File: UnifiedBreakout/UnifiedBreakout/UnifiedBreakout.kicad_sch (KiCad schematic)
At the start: 29 parts, among them J6 24V BUS, J7 DRAWBAR+MIST+AXIS_PWR, J8 LIMIT, J9 AUX, U4 G3VM-61A1, U5 G3VM-61A1, U6 G3VM-61A1, U7 4N35

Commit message: V3 BOM
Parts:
- C2, C4: Farnell PN (none) -> 8126585; MPN 860080574007 -> 35RX30100M8X11.5; Manufacturer Wurth Elektronik -> Rubycon
- R11, R12, R16: Farnell PN (none) -> 9341528; MPN CFR-25JB-52-220R -> MF25 220R; Manufacturer Yageo -> MULTICOMP PRO
- R13, R14, R15, R18: Farnell PN (none) -> 9341536; MPN CFR-25JB-52-2K2 -> MF25 2K2; Manufacturer Yageo -> MULTICOMP PRO
- R17: Farnell PN (none) -> 9341552; MPN CFR-25JB-52-220K -> MF25 220K; Manufacturer Yageo -> MULTICOMP PRO
- U4, U5, U6: MPN (none) -> G3VM-61A1; Manufacturer (none) -> Omron
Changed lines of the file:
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@@
       (effects (font (size 1.27 1.27)) hide)
     )
-    (property "MPN" "860080574007" (at 124.46 270.51 0)
-      (effects (font (size 1.27 1.27)) hide)
-    )
-    (property "Manufacturer" "Wurth Elektronik" (at 124.46 270.51 0)
-      (effects (font (size 1.27 1.27)) hide)
-    )
-    (property "Farnell PN" "" (at 124.46 270.51 0)
+    (property "MPN" "35RX30100M8X11.5 " (at 124.46 270.51 0)
+      (effects (font (size 1.27 1.27)) hide)
+    )
+    (property "Manufacturer" "Rubycon" (at 124.46 270.51 0)
+      (effects (font (size 1.27 1.27)) hide)
+    )
+    (property "Farnell PN" "8126585" (at 124.46 270.51 0)
       (effects (font (size 1.27 1.27)) hide)
     )
@@
       (effects (font (size 1.27 1.27)) hide)
     )
-    (property "MPN" "860080574007" (at 175.26 270.51 0)
-      (effects (font (size 1.27 1.27)) hide)
-    )
-    (property "Manufacturer" "Wurth Elektronik" (at 175.26 270.51 0)
-      (effects (font (size 1.27 1.27)) hide)
-    )
-    (property "Farnell PN" "" (at 175.26 270.51 0)
+    (property "MPN" "35RX30100M8X11.5 " (at 175.26 270.51 0)
+      (effects (font (size 1.27 1.27)) hide)
+    )
+    (property "Manufacturer" "Rubycon" (at 175.26 270.51 0)
+      (effects (font (size 1.27 1.27)) hide)
+    )
+    (property "Farnell PN" "8126585" (at 175.26 270.51 0)
       (effects (font (size 1.27 1.27)) hide)
     )
@@
       (effects (font (size 1.27 1.27)) hide)
     )
-    (property "MPN" "CFR-25JB-52-220R" (at 26.67 63.5 0)
-      (effects (font (size 1.27 1.27)) hide)
-    )
-    (property "Manufacturer" "Yageo" (at 26.67 63.5 0)
-      (effects (font (size 1.27 1.27)) hide)
-    )
-    (property "Farnell PN" "" (at 26.67 63.5 0)
+    (property "MPN" "MF25 220R" (at 26.67 63.5 0)
+      (effects (font (size 1.27 1.27)) hide)
+    )
+    (property "Manufacturer" "MULTICOMP PRO" (at 26.67 63.5 0)
+      (effects (font (size 1.27 1.27)) hide)
+    )
+    (property "Farnell PN" "9341528" (at 26.67 63.5 0)
       (effects (font (size 1.27 1.27)) hide)
     )
@@
       (effects (font (size 1.27 1.27)) hide)
     )
-    (property "MPN" "CFR-25JB-52-220R" (at 30.48 134.62 0)
-      (effects (font (size 1.27 1.27)) hide)
-    )
-    (property "Manufacturer" "Yageo" (at 30.48 134.62 0)
-      (effects (font (size 1.27 1.27)) hide)
-    )
-    (property "Farnell PN" "" (at 30.48 134.62 0)
+    (property "MPN" "MF25 220R" (at 30.48 134.62 0)
+      (effects (font (size 1.27 1.27)) hide)
+    )
+    (property "Manufacturer" "MULTICOMP PRO" (at 30.48 134.62 0)
+      (effects (font (size 1.27 1.27)) hide)
+    )
+    (property "Farnell PN" "9341528" (at 30.48 134.62 0)
       (effects (font (size 1.27 1.27)) hide)
     )
@@
       (effects (font (size 1.27 1.27)) hide)
     )
-    (property "MPN" "CFR-25JB-52-220K" (at 298.45 212.09 0)
-      (effects (font (size 1.27 1.27)) hide)
-    )
-    (property "Manufacturer" "Yageo" (at 298.45 212.09 0)
-      (effects (font (size 1.27 1.27)) hide)
-    )
-    (property "Farnell PN" "" (at 298.45 212.09 0)
+    (property "MPN" "MF25 220K" (at 298.45 212.09 0)
+      (effects (font (size 1.27 1.27)) hide)
+    )
+    (property "Manufacturer" "MULTICOMP PRO" (at 298.45 212.09 0)
+      (effects (font (size 1.27 1.27)) hide)
+    )
+    (property "Farnell PN" "9341552" (at 298.45 212.09 0)
       (effects (font (size 1.27 1.27)) hide)
     )
@@
       (effects (font (size 1.27 1.27)) hide)
     )
-    (property "MPN" "CFR-25JB-52-2K2" (at 327.66 205.74 0)
-      (effects (font (size 1.27 1.27)) hide)
-    )
-    (property "Manufacturer" "Yageo" (at 327.66 205.74 0)
-      (effects (font (size 1.27 1.27)) hide)
-    )
-    (property "Farnell PN" "" (at 327.66 205.74 0)
+    (property "MPN" "MF25 2K2" (at 327.66 205.74 0)
+      (effects (font (size 1.27 1.27)) hide)
+    )
+    (property "Manufacturer" "MULTICOMP PRO" (at 327.66 205.74 0)
+      (effects (font (size 1.27 1.27)) hide)
+    )
+    (property "Farnell PN" "9341536" (at 327.66 205.74 0)
       (effects (font (size 1.27 1.27)) hide)
     )
@@
       (effects (font (size 1.27 1.27)) hide)
     )
-    (property "MPN" "CFR-25JB-52-2K2" (at 43.18 187.96 0)
-      (effects (font (size 1.27 1.27)) hide)
-    )
-    (property "Manufacturer" "Yageo" (at 43.18 187.96 0)
-      (effects (font (size 1.27 1.27)) hide)
-    )
-    (property "Farnell PN" "" (at 43.18 187.96 0)
+    (property "MPN" "MF25 2K2" (at 43.18 187.96 0)
+      (effects (font (size 1.27 1.27)) hide)
+    )
+    (property "Manufacturer" "MULTICOMP PRO" (at 43.18 187.96 0)
+      (effects (font (size 1.27 1.27)) hide)
+    )
+    (property "Farnell PN" "9341536" (at 43.18 187.96 0)
       (effects (font (size 1.27 1.27)) hide)
     )
@@
       (effects (font (size 1.27 1.27)) hide)
     )
+    (property "MPN" "G3VM-61A1" (at 58.42 190.5 0)
+      (effects (font (size 1.27 1.27)) hide)
+    )
+    (property "Manufacturer" "Omron" (at 58.42 190.5 0)
+      (effects (font (size 1.27 1.27)) hide)
+    )
     (pin "1")
     (pin "2")
@@
       (effects (font (size 1.27 1.27)) hide)
     )
-    (property "MPN" "CFR-25JB-52-2K2" (at 43.18 207.01 0)
-      (effects (font (size 1.27 1.27)) hide)
-    )
-    (property "Manufacturer" "Yageo" (at 43.18 207.01 0)
-      (effects (font (size 1.27 1.27)) hide)
-    )
-    (property "Farnell PN" "" (at 43.18 207.01 0)
+    (property "MPN" "MF25 2K2" (at 43.18 207.01 0)
+      (effects (font (size 1.27 1.27)) hide)
+    )
+    (property "Manufacturer" "MULTICOMP PRO" (at 43.18 207.01 0)
+      (effects (font (size 1.27 1.27)) hide)
+    )
+    (property "Farnell PN" "9341536" (at 43.18 207.01 0)
       (effects (font (size 1.27 1.27)) hide)
     )
@@
       (effects (font (size 1.27 1.27)) hide)
     )
+    (property "MPN" "G3VM-61A1" (at 58.42 209.55 0)
+      (effects (font (size 1.27 1.27)) hide)
+    )
+    (property "Manufacturer" "Omron" (at 58.42 209.55 0)
+      (effects (font (size 1.27 1.27)) hide)
+    )
     (pin "1")
     (pin "2")
@@
       (effects (font (size 1.27 1.27)) hide)
     )
-    (property "MPN" "CFR-25JB-52-2K2" (at 43.18 226.06 0)
-      (effects (font (size 1.27 1.27)) hide)
-    )
-    (property "Manufacturer" "Yageo" (at 43.18 226.06 0)
-      (effects (font (size 1.27 1.27)) hide)
-    )
-    (property "Farnell PN" "" (at 43.18 226.06 0)
+    (property "MPN" "MF25 2K2" (at 43.18 226.06 0)
+      (effects (font (size 1.27 1.27)) hide)
+    )
+    (property "Manufacturer" "MULTICOMP PRO" (at 43.18 226.06 0)
+      (effects (font (size 1.27 1.27)) hide)
+    )
+    (property "Farnell PN" "9341536" (at 43.18 226.06 0)
       (effects (font (size 1.27 1.27)) hide)
     )
@@
       (effects (font (size 1.27 1.27)) hide)
     )
-    (property "MPN" "CFR-25JB-52-220R" (at 76.2 260.35 0)
-      (effects (font (size 1.27 1.27)) hide)
-    )
-    (property "Manufacturer" "Yageo" (at 76.2 260.35 0)
-      (effects (font (size 1.27 1.27)) hide)
-    )
-    (property "Farnell PN" "" (at 76.2 260.35 0)
+    (property "MPN" "MF25 220R" (at 76.2 260.35 0)
+      (effects (font (size 1.27 1.27)) hide)
+    )
+    (property "Manufacturer" "MULTICOMP PRO" (at 76.2 260.35 0)
+      (effects (font (size 1.27 1.27)) hide)
+    )
+    (property "Farnell PN" "9341528" (at 76.2 260.35 0)
       (effects (font (size 1.27 1.27)) hide)
     )
@@
       (effects (font (size 1.27 1.27)) hide)
     )
+    (property "MPN" "G3VM-61A1" (at 58.42 228.6 0)
+      (effects (font (size 1.27 1.27)) hide)
+    )
+    (property "Manufacturer" "Omron" (at 58.42 228.6 0)
+      (effects (font (size 1.27 1.27)) hide)
+    )

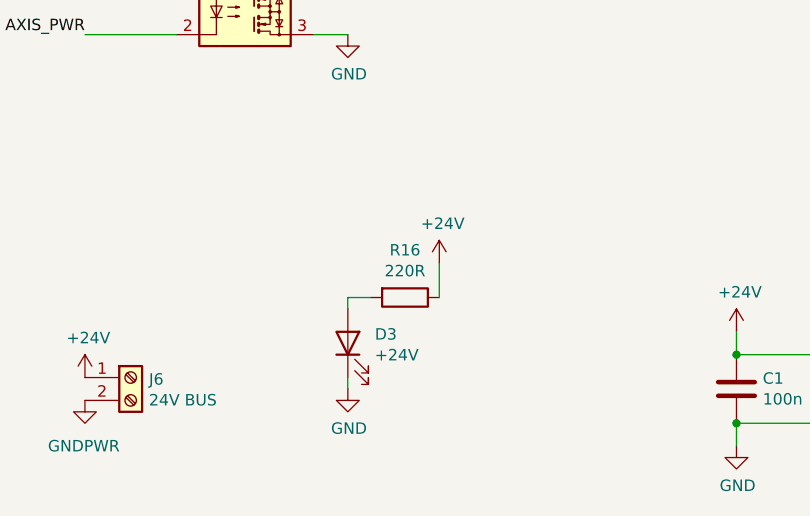
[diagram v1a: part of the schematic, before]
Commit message: Use 2k2 resistor for 24V power LED
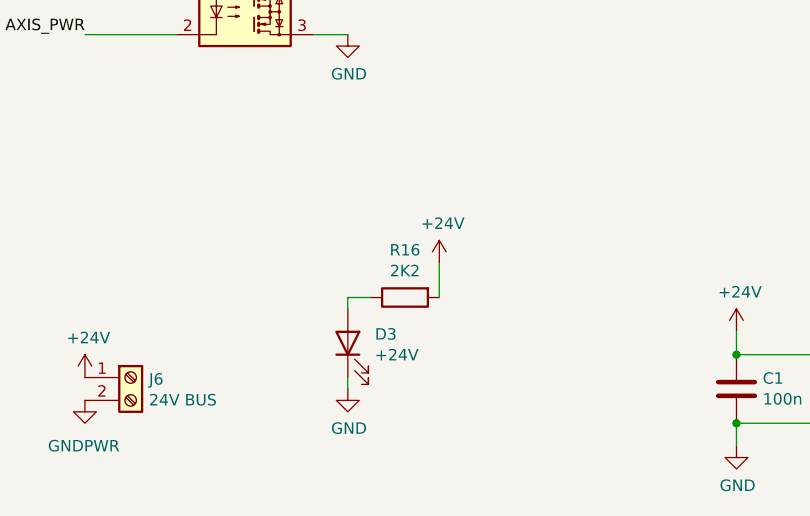
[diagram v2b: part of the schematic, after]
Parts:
- R16: value 220R -> 2K2; Farnell PN 9341528 -> 9341536; MPN MF25 220R -> MF25 2K2
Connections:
- net +24V: now also R16.2; no longer R16.1
- net at D3.2 (A): now also R16.1; no longer R16.2
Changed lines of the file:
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@@
+    )
+  )
+  (symbol (lib_id "Device:R") (at 76.2 260.35 90) (mirror x) (unit 1)
+    (in_bom yes) (on_board yes) (dnp no)
+    (property "Reference" "R16" (at 76.2 255.0922 90)
+      (effects (font (size 1.27 1.27)))
+    )
+    (property "Value" "2K2" (at 76.2 257.4036 90)
+      (effects (font (size 1.27 1.27)))
+    )
+    (property "Footprint" "Resistor_THT:R_Axial_DIN0207_L6.3mm_D2.5mm_P7.62mm_Horizontal" (at 76.2 258.572 90)
+      (effects (font (size 1.27 1.27)) hide)
+    )
+    (property "Datasheet" "~" (at 76.2 260.35 0)
+      (effects (font (size 1.27 1.27)) hide)
+    )
+    (property "MPN" "MF25 2K2" (at 76.2 260.35 0)
+      (effects (font (size 1.27 1.27)) hide)
+    )
+    (property "Manufacturer" "MULTICOMP PRO" (at 76.2 260.35 0)
+      (effects (font (size 1.27 1.27)) hide)
+    )
+    (property "Farnell PN" "9341536" (at 76.2 260.35 0)
+      (effects (font (size 1.27 1.27)) hide)
+    )
+    (pin "1")
+    (pin "2")
+    (instances
+      (project "UnifiedBreakout"
+        (path "/e63e39d7-6ac0-4ffd-8aa3-1841a4541b55"
+          (reference "R16") (unit 1)
+        )
+      )
     )
   )
@@
         )
       )
-    )
-  )
-  (symbol (lib_id "Device:R") (at 76.2 260.35 270) (unit 1)
-    (in_bom yes) (on_board yes) (dnp no)
-    (property "Reference" "R16" (at 76.2 255.0922 90)
-      (effects (font (size 1.27 1.27)))
-    )
-    (property "Value" "220R" (at 76.2 257.4036 90)
-      (effects (font (size 1.27 1.27)))
-    )
-    (property "Footprint" "Resistor_THT:R_Axial_DIN0207_L6.3mm_D2.5mm_P7.62mm_Horizontal" (at 76.2 258.572 90)
-      (effects (font (size 1.27 1.27)) hide)
-    )
-    (property "Datasheet" "~" (at 76.2 260.35 0)
-      (effects (font (size 1.27 1.27)) hide)
-    )
-    (property "MPN" "MF25 220R" (at 76.2 260.35 0)
-      (effects (font (size 1.27 1.27)) hide)
-    )
-    (property "Manufacturer" "MULTICOMP PRO" (at 76.2 260.35 0)
-      (effects (font (size 1.27 1.27)) hide)
-    )
-    (property "Farnell PN" "9341528" (at 76.2 260.35 0)
-      (effects (font (size 1.27 1.27)) hide)
-    )
-    (pin "1")
-    (pin "2")
-    (instances
-      (project "UnifiedBreakout"
-        (path "/e63e39d7-6ac0-4ffd-8aa3-1841a4541b55"
-          (reference "R16") (unit 1)
-        )
-      )

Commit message: v3.1
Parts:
- R13, R14, R15: value 2K2 -> 680R; Farnell PN 9341536 -> 9342150; MPN MF25 2K2 -> MF25 680R
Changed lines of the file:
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@@
       (effects (font (size 1.27 1.27)))
     )
-    (property "Value" "2K2" (at 43.18 185.0136 90)
+    (property "Value" "680R" (at 43.18 185.0136 90)
       (effects (font (size 1.27 1.27)))
     )
@@
       (effects (font (size 1.27 1.27)) hide)
     )
-    (property "MPN" "MF25 2K2" (at 43.18 187.96 0)
+    (property "MPN" "MF25 680R" (at 43.18 187.96 0)
       (effects (font (size 1.27 1.27)) hide)
     )
@@
       (effects (font (size 1.27 1.27)) hide)
     )
-    (property "Farnell PN" "9341536" (at 43.18 187.96 0)
+    (property "Farnell PN" "9342150" (at 43.18 187.96 0)
       (effects (font (size 1.27 1.27)) hide)
     )
@@
         (path "/e63e39d7-6ac0-4ffd-8aa3-1841a4541b55"
           (reference "R13") (unit 1)
+        )
+      )
+    )
+  )
+  (symbol (lib_id "Device:R") (at 43.18 207.01 90) (mirror x) (unit 1)
+    (in_bom yes) (on_board yes) (dnp no)
+    (property "Reference" "R14" (at 43.18 201.7522 90)
+      (effects (font (size 1.27 1.27)))
+    )
+    (property "Value" "680R" (at 43.18 204.0636 90)
+      (effects (font (size 1.27 1.27)))
+    )
+    (property "Footprint" "Resistor_THT:R_Axial_DIN0207_L6.3mm_D2.5mm_P7.62mm_Horizontal" (at 43.18 205.232 90)
+      (effects (font (size 1.27 1.27)) hide)
+    )
+    (property "Datasheet" "~" (at 43.18 207.01 0)
+      (effects (font (size 1.27 1.27)) hide)
+    )
+    (property "MPN" "MF25 680R" (at 43.18 207.01 0)
+      (effects (font (size 1.27 1.27)) hide)
+    )
+    (property "Manufacturer" "MULTICOMP PRO" (at 43.18 207.01 0)
+      (effects (font (size 1.27 1.27)) hide)
+    )
+    (property "Farnell PN" "9342150" (at 43.18 207.01 0)
+      (effects (font (size 1.27 1.27)) hide)
+    )
+    (pin "1")
+    (pin "2")
+    (instances
+      (project "UnifiedBreakout"
+        (path "/e63e39d7-6ac0-4ffd-8aa3-1841a4541b55"
+          (reference "R14") (unit 1)
         )
       )
@@
     )
   )
-  (symbol (lib_id "Device:R") (at 43.18 207.01 90) (mirror x) (unit 1)
-    (in_bom yes) (on_board yes) (dnp no)
-    (property "Reference" "R14" (at 43.18 201.7522 90)
-      (effects (font (size 1.27 1.27)))
-    )
-    (property "Value" "2K2" (at 43.18 204.0636 90)
-      (effects (font (size 1.27 1.27)))
-    )
-    (property "Footprint" "Resistor_THT:R_Axial_DIN0207_L6.3mm_D2.5mm_P7.62mm_Horizontal" (at 43.18 205.232 90)
-      (effects (font (size 1.27 1.27)) hide)
-    )
-    (property "Datasheet" "~" (at 43.18 207.01 0)
-      (effects (font (size 1.27 1.27)) hide)
-    )
-    (property "MPN" "MF25 2K2" (at 43.18 207.01 0)
-      (effects (font (size 1.27 1.27)) hide)
-    )
-    (property "Manufacturer" "MULTICOMP PRO" (at 43.18 207.01 0)
-      (effects (font (size 1.27 1.27)) hide)
-    )
-    (property "Farnell PN" "9341536" (at 43.18 207.01 0)
-      (effects (font (size 1.27 1.27)) hide)
-    )
-    (pin "1")
-    (pin "2")
-    (instances
-      (project "UnifiedBreakout"
-        (path "/e63e39d7-6ac0-4ffd-8aa3-1841a4541b55"
-          (reference "R14") (unit 1)
-        )
-      )
-    )
-  )
   (symbol (lib_id "Mechanical:MountingHole_Pad") (at 228.6 264.16 0) (unit 1)
     (in_bom yes) (on_board yes) (dnp no)
@@
         (path "/e63e39d7-6ac0-4ffd-8aa3-1841a4541b55"
           (reference "#PWR020") (unit 1)
+        )
+      )
+    )
+  )
+  (symbol (lib_id "Device:R") (at 43.18 226.06 90) (mirror x) (unit 1)
+    (in_bom yes) (on_board yes) (dnp no)
+    (property "Reference" "R15" (at 43.18 220.8022 90)
+      (effects (font (size 1.27 1.27)))
+    )
+    (property "Value" "680R" (at 43.18 223.1136 90)
+      (effects (font (size 1.27 1.27)))
+    )
+    (property "Footprint" "Resistor_THT:R_Axial_DIN0207_L6.3mm_D2.5mm_P7.62mm_Horizontal" (at 43.18 224.282 90)
+      (effects (font (size 1.27 1.27)) hide)
+    )
+    (property "Datasheet" "~" (at 43.18 226.06 0)
+      (effects (font (size 1.27 1.27)) hide)
+    )
+    (property "MPN" "MF25 680R" (at 43.18 226.06 0)
+      (effects (font (size 1.27 1.27)) hide)
+    )
+    (property "Manufacturer" "MULTICOMP PRO" (at 43.18 226.06 0)
+      (effects (font (size 1.27 1.27)) hide)
+    )
+    (property "Farnell PN" "9342150" (at 43.18 226.06 0)
+      (effects (font (size 1.27 1.27)) hide)
+    )
+    (pin "1")
+    (pin "2")
+    (instances
+      (project "UnifiedBreakout"
+        (path "/e63e39d7-6ac0-4ffd-8aa3-1841a4541b55"
+          (reference "R15") (unit 1)
         )
       )
@@
         )
       )
-    )
-  )
-  (symbol (lib_id "Device:R") (at 43.18 226.06 90) (mirror x) (unit 1)
-    (in_bom yes) (on_board yes) (dnp no)
-    (property "Reference" "R15" (at 43.18 220.8022 90)
-      (effects (font (size 1.27 1.27)))
-    )
-    (property "Value" "2K2" (at 43.18 223.1136 90)
-      (effects (font (size 1.27 1.27)))
-    )
-    (property "Footprint" "Resistor_THT:R_Axial_DIN0207_L6.3mm_D2.5mm_P7.62mm_Horizontal" (at 43.18 224.282 90)
-      (effects (font (size 1.27 1.27)) hide)
-    )
-    (property "Datasheet" "~" (at 43.18 226.06 0)
-      (effects (font (size 1.27 1.27)) hide)
-    )
-    (property "MPN" "MF25 2K2" (at 43.18 226.06 0)
-      (effects (font (size 1.27 1.27)) hide)
-    )
-    (property "Manufacturer" "MULTICOMP PRO" (at 43.18 226.06 0)
-      (effects (font (size 1.27 1.27)) hide)
-    )
-    (property "Farnell PN" "9341536" (at 43.18 226.06 0)
-      (effects (font (size 1.27 1.27)) hide)
-    )
-    (pin "1")
-    (pin "2")
-    (instances
-      (project "UnifiedBreakout"
-        (path "/e63e39d7-6ac0-4ffd-8aa3-1841a4541b55"
-          (reference "R15") (unit 1)
-        )
-      )
